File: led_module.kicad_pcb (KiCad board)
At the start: 2 copper layers, 52.1 x 34.3 mm, 8 parts, among them J1 Conn_02x20_Odd_Even, Q1 2N7000, Q2 2N7000, Q3 2N7000, Q4 2N7000

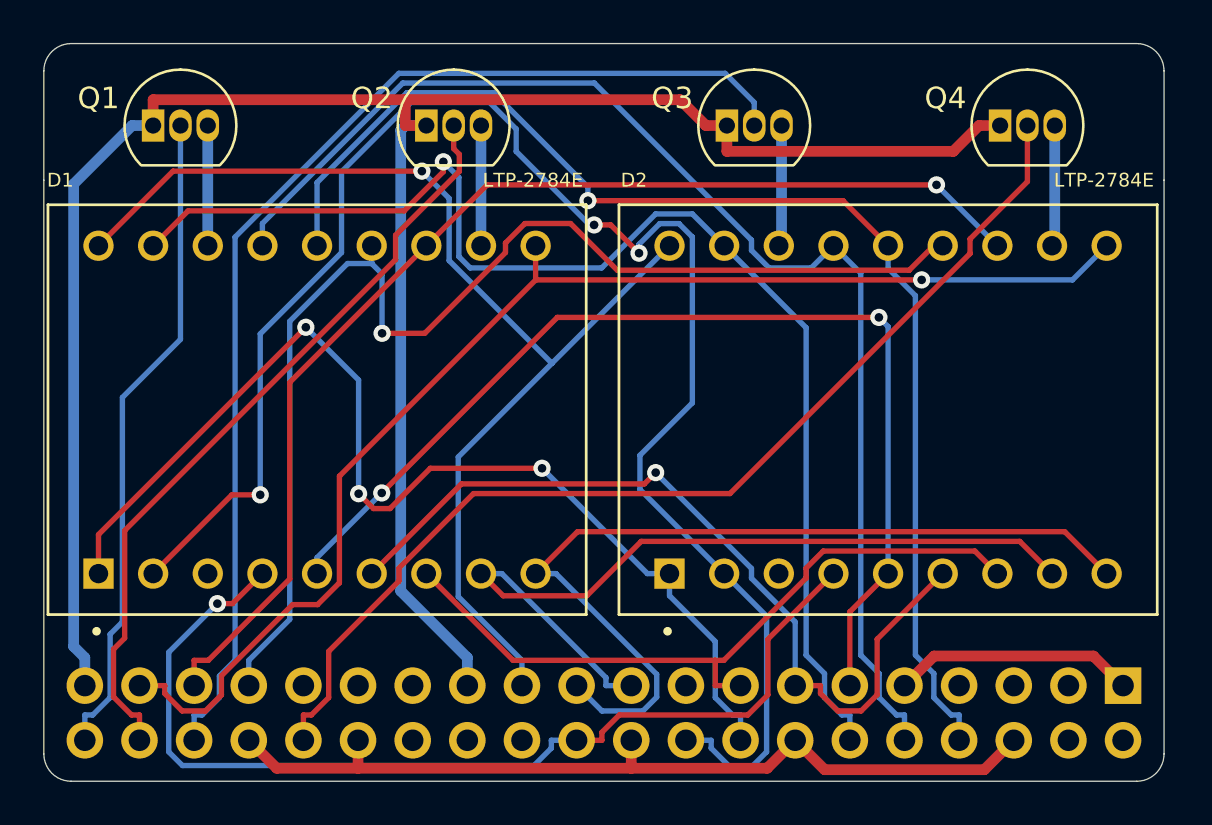
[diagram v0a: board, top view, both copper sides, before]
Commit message: Update to rev C.  Pin 1 was connected to ground (based on user manual).  It is actually connected to 3V3 and is not connected in rev C.  Change the footprint for Q1-Q4 to 2.54mm pin spacing to make hand soldering easier.  Add text on back side.
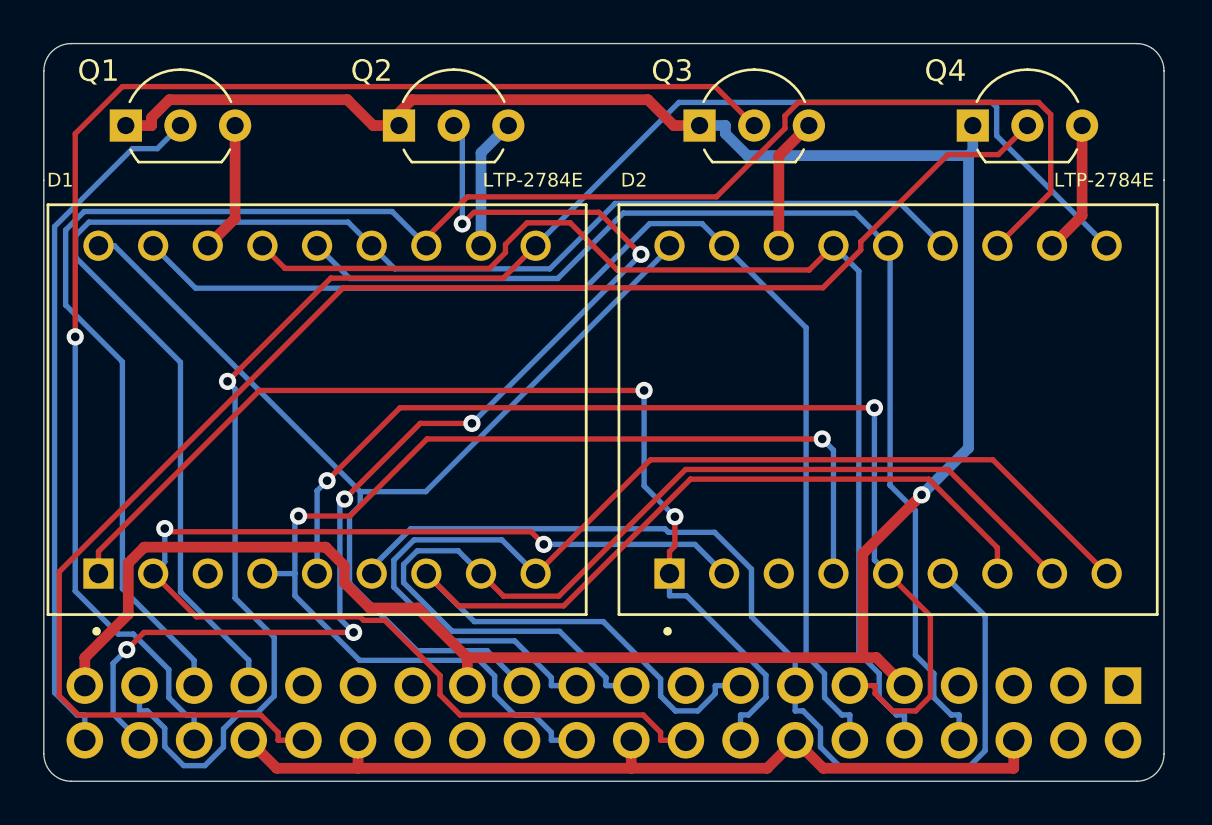
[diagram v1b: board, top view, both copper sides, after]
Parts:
- removed the REF** at (53.3, 114.3)
- added REF**: OSHW-Logo2_14.6x12mm_SilkScreen, Symbol:OSHW-Logo2_14.6x12mm_SilkScreen, B.Cu at (69.8, 113.0)
- Q1, Q2, Q3, Q4: footprint Package_TO_SOT_THT:TO-92_Inline -> Package_TO_SOT_THT:TO-92L_Inline_Wide
- moved Q1 1.27 mm to (31.8, 100.3)
- moved Q2 1.27 mm to (44.5, 100.3)
- moved Q3 1.27 mm to (58.4, 100.3)
- moved Q4 1.27 mm to (71.1, 100.3)
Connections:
- J1 pad 1: GND -> (no net)
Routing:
- net Net-(D1-Pad12): track 54.2 -> 81.1 mm, vias 1 -> 0
- net Net-(J1-Pad32): track 49.7 -> 72.0 mm
- net Net-(D1-Pad2): track 77.4 -> 57.9 mm, vias 3 -> 2
- net Net-(J1-Pad38): track 36.1 -> 55.0 mm, vias 0 -> 6
- net Net-(D1-Pad7): track 33.4 -> 50.5 mm
- net Net-(D1-Pad10): track 59.6 -> 76.1 mm
- net Net-(D1-Pad8): track 38.0 -> 49.3 mm
- net Net-(D1-Pad13): track 56.7 -> 67.8 mm, vias 1 -> 0
- net Net-(J1-Pad36): track 53.3 -> 64.3 mm, vias 0 -> 1
- net Net-(D1-Pad9): track 41.3 -> 50.4 mm
- net Net-(D1-Pad6): track 39.5 -> 46.6 mm, vias 1 -> 0
- net Net-(D1-Pad4): track 47.3 -> 54.2 mm, vias 1 -> 2
- net Net-(D1-Pad14): track 59.1 -> 53.6 mm, vias 1 -> 0
- net Net-(D1-Pad17): track 59.9 -> 54.7 mm, vias 1 -> 0
- net Net-(D1-Pad15): track 59.1 -> 54.0 mm
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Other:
- board text added: "14-Segment LED Module for Pynq-Z2 RPi Header Rev C"

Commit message: Small update to 14-segment display board.
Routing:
- added copper zone on B.Cu, net (none)
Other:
- board text added: "®©®"
